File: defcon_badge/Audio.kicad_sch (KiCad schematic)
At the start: 16 parts, among them J20 PJ-320A, U20 TM8211, U21 TDA1308

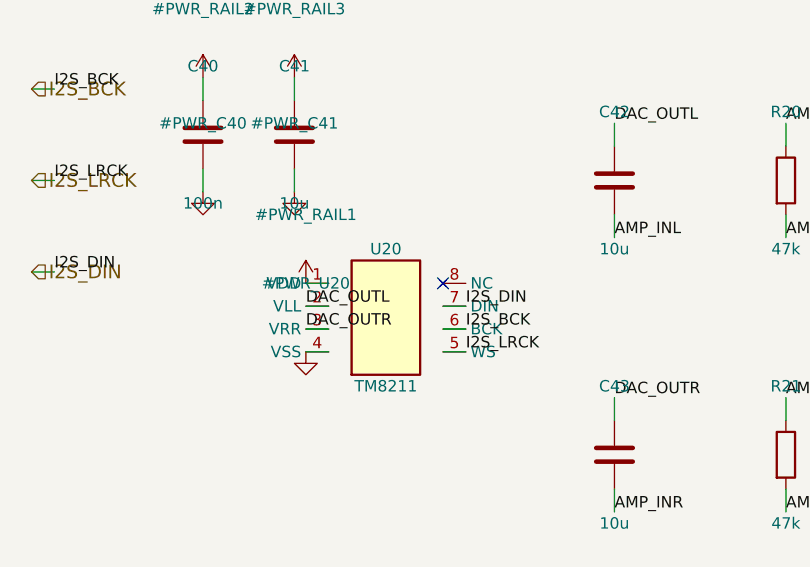
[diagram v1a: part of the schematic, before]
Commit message: Schematic: fix TM8211 DAC + SK9822 LED pinouts (datasheet-verified)
Both were ERC-invisible symbol bugs (wrong pin-number->signal mapping) that only
datasheet cross-reference catches — the kind that ships a non-functional board.

- TM8211 DAC (U20): the symbol pinout was scrambled. Verified against the Princeton
  PT8211 datasheet (+3 cross-checks): 1=BCK 2=WS 3=DIN 4=GND 5=VDD 6=LCH 7=NC 8=RCH.
  Fixed both symbol defs (gen_badge_lib + the inline copy in gen_audio_sheet) AND
  re-mapped the U20 wiring. Netlist verified: +3V3 was landing on the bit-clock pad;
  now every I2S/analog pin is on the correct pad.
- SK9822 LEDs (LED20-23): symbol pinout scrambled AND a 4-pad SK6812 footprint on a
  6-pin part. User chose 5050 (large/bright). Verified the SK9822 5050 datasheet
  pinout (Adafruit/Pololu/Normand): 1=DIN 2=CIN 3=GND 4=VDD 5=COUT 6=DOUT. Fixed the
  symbol + re-mapped the chain wiring; netlist verified (DOUT->next DIN, COUT->next
  CIN linked). Footprint set to badge:LED_SK9822_5050 — the 6-pad 5050 land pattern
  must be created in the PCB phase (no stock KiCad addressable-5050 footprint).
- Verified W25Q16 flash is a false alarm (already correct USON-8 + pinout).

ERC still 0 errors. The +4 warnings are the deliberate SK9822-footprint TODO.

Co-Authored-By: Claude Opus 4.8 (1M context) <noreply@anthropic.com>
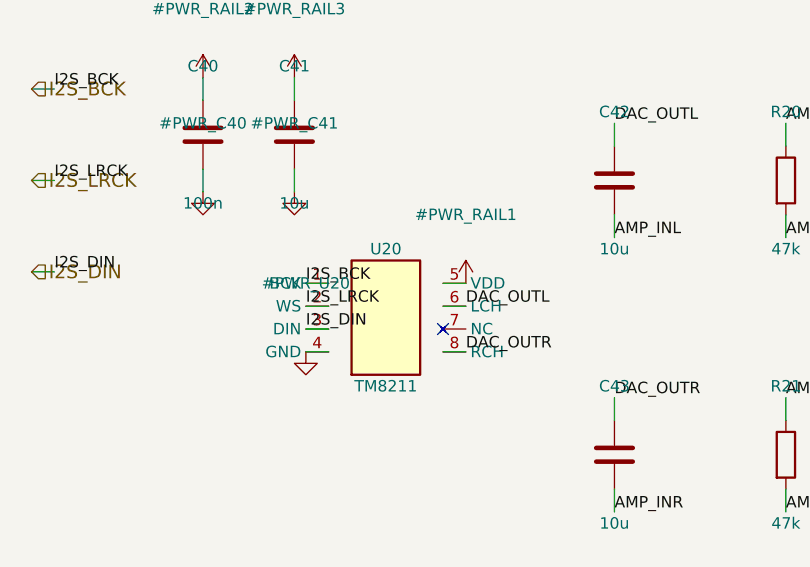
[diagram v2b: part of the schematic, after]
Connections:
- net +3V3: now also U20.5 (VDD); no longer U20.1 (VDD)
- net DAC_OUTL: now also U20.6 (LCH); no longer U20.2 (VLL)
- net DAC_OUTR: now also U20.8 (RCH); no longer U20.3 (VRR)
- net I2S_BCK: now also U20.1 (BCK); no longer U20.6 (BCK)
- net I2S_DIN: now also U20.3 (DIN); no longer U20.7 (DIN)
- net I2S_LRCK: now also U20.2 (WS); no longer U20.5 (WS)
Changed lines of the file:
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@@
 		(pin "3")
 		(pin "4")
+		(pin "5")
+		(pin "6")
+		(pin "7")
 		(pin "8")
-		(pin "7")
-		(pin "6")
-		(pin "5")
 		(instances
 			(project "defcon_badge"
@@
 	(symbol
 		(lib_id "power:+3V3")
-		(at 66.04 76.20 0)
-		(unit 1)
-		(body_style 1)
-		(exclude_from_sim no)
-		(in_bom yes)
-		(on_board yes)
-		(in_pos_files yes)
-		(dnp no)
-		(fields_autoplaced yes)
-		(property "Reference" "#PWR_RAIL1" (at 66.04 68.58 0) (effects (font (size 1.27 1.27))))
-		(property "Value" "+3V3" (at 66.04 83.82 0) (effects (font (size 1.27 1.27)) (hide yes)))
-		(property "Footprint" "" (at 66.04 76.20 0) (show_name no) (hide yes) (effects (font (size 1.27 1.27))))
-		(property "Datasheet" "" (at 66.04 76.20 0) (show_name no) (hide yes) (effects (font (size 1.27 1.27))))
-		(property "Description" "" (at 66.04 76.20 0) (show_name no) (hide yes) (effects (font (size 1.27 1.27))))
+		(at 83.82 76.20 0)
+		(unit 1)
+		(body_style 1)
+		(exclude_from_sim no)
+		(in_bom yes)
+		(on_board yes)
+		(in_pos_files yes)
+		(dnp no)
+		(fields_autoplaced yes)
+		(property "Reference" "#PWR_RAIL1" (at 83.82 68.58 0) (effects (font (size 1.27 1.27))))
+		(property "Value" "+3V3" (at 83.82 83.82 0) (effects (font (size 1.27 1.27)) (hide yes)))
+		(property "Footprint" "" (at 83.82 76.20 0) (show_name no) (hide yes) (effects (font (size 1.27 1.27))))
+		(property "Datasheet" "" (at 83.82 76.20 0) (show_name no) (hide yes) (effects (font (size 1.27 1.27))))
+		(property "Description" "" (at 83.82 76.20 0) (show_name no) (hide yes) (effects (font (size 1.27 1.27))))
 		(pin "1")
 		(instances
@@
 		)
 	)
-	(wire (pts (xy 68.58 76.20) (xy 66.04 76.20)) (stroke (width 0) (type default)))
+	(wire (pts (xy 81.28 76.20) (xy 83.82 76.20)) (stroke (width 0) (type default)))
 	(wire (pts (xy 68.58 83.82) (xy 66.04 83.82)) (stroke (width 0) (type default)))
 	(wire (pts (xy 54.61 55.88) (xy 54.61 53.34)) (stroke (width 0) (type default)))
@@
 	(wire (pts (xy 64.77 55.88) (xy 64.77 53.34)) (stroke (width 0) (type default)))
 	(wire (pts (xy 64.77 63.50) (xy 64.77 66.04)) (stroke (width 0) (type default)))
-	(wire (pts (xy 81.28 81.28) (xy 83.82 81.28)) (stroke (width 0) (type default)))
-	(wire (pts (xy 81.28 83.82) (xy 83.82 83.82)) (stroke (width 0) (type default)))
-	(wire (pts (xy 81.28 78.74) (xy 83.82 78.74)) (stroke (width 0) (type default)))
+	(wire (pts (xy 68.58 76.20) (xy 66.04 76.20)) (stroke (width 0) (type default)))
 	(wire (pts (xy 68.58 78.74) (xy 66.04 78.74)) (stroke (width 0) (type default)))
 	(wire (pts (xy 68.58 81.28) (xy 66.04 81.28)) (stroke (width 0) (type default)))
+	(wire (pts (xy 81.28 78.74) (xy 83.82 78.74)) (stroke (width 0) (type default)))
+	(wire (pts (xy 81.28 83.82) (xy 83.82 83.82)) (stroke (width 0) (type default)))
 	(wire (pts (xy 100.33 60.96) (xy 100.33 58.42)) (stroke (width 0) (type default)))
 	(wire (pts (xy 100.33 68.58) (xy 100.33 71.12)) (stroke (width 0) (type default)))
@@
 	(wire (pts (xy 35.56 64.77) (xy 38.10 64.77)) (stroke (width 0) (type default)))
 	(wire (pts (xy 35.56 74.93) (xy 38.10 74.93)) (stroke (width 0) (type default)))
-	(no_connect (at 81.28 76.20))
+	(no_connect (at 81.28 81.28))
 	(no_connect (at 208.28 77.47))
 	(no_connect (at 208.28 82.55))
-	(label "I2S_BCK" (at 83.82 81.28 0) (effects (font (size 1.27 1.27)) (justify left bottom)))
-	(label "I2S_LRCK" (at 83.82 83.82 0) (effects (font (size 1.27 1.27)) (justify left bottom)))
-	(label "I2S_DIN" (at 83.82 78.74 0) (effects (font (size 1.27 1.27)) (justify left bottom)))
-	(label "DAC_OUTL" (at 66.04 78.74 0) (effects (font (size 1.27 1.27)) (justify left bottom)))
-	(label "DAC_OUTR" (at 66.04 81.28 0) (effects (font (size 1.27 1.27)) (justify left bottom)))
+	(label "I2S_BCK" (at 66.04 76.20 0) (effects (font (size 1.27 1.27)) (justify left bottom)))
+	(label "I2S_LRCK" (at 66.04 78.74 0) (effects (font (size 1.27 1.27)) (justify left bottom)))
+	(label "I2S_DIN" (at 66.04 81.28 0) (effects (font (size 1.27 1.27)) (justify left bottom)))
+	(label "DAC_OUTL" (at 83.82 78.74 0) (effects (font (size 1.27 1.27)) (justify left bottom)))
+	(label "DAC_OUTR" (at 83.82 83.82 0) (effects (font (size 1.27 1.27)) (justify left bottom)))
 	(label "DAC_OUTL" (at 100.33 58.42 0) (effects (font (size 1.27 1.27)) (justify left bottom)))
 	(label "AMP_INL" (at 100.33 71.12 0) (effects (font (size 1.27 1.27)) (justify left bottom)))

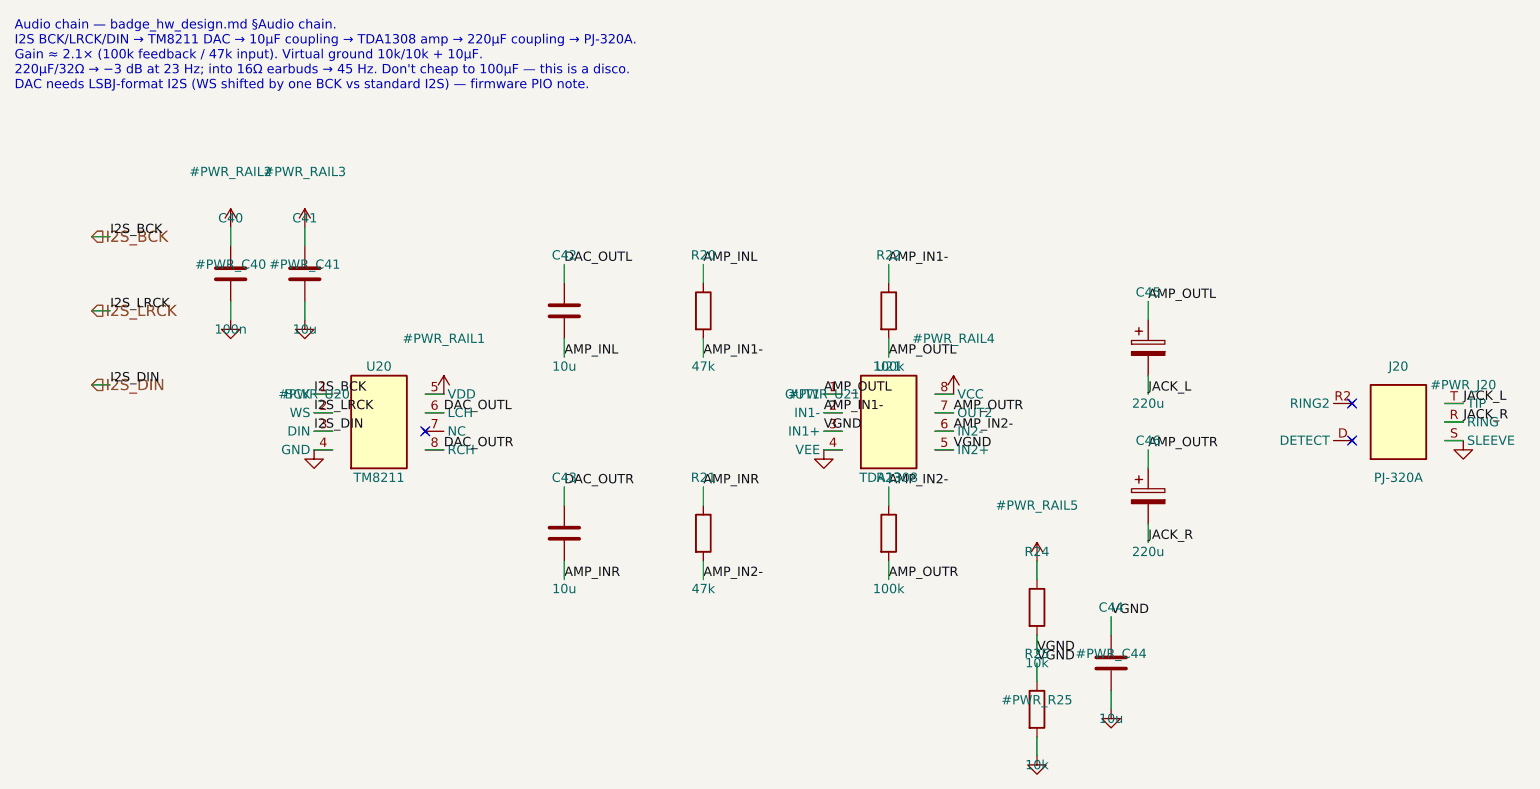
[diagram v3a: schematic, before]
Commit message: PCB: stereo audio jack + decoupling/thermal/clearance/placement fixes
J20 audio jack: the schematic specified a Thonkiconn WQP-PJ398SM footprint,
which is MONO (S/T/TN only) — wrong for a stereo badge (JACK_R had nowhere
to land). Swapped to CUI SJ1-3523N, a mainstream through-hole stereo TRS
jack with a verified KiCad footprint (TH survives plug/unplug better than
SMD). T=JACK_L, R=JACK_R, S=GND. Placed barrel overhanging the top edge,
repositioned to clear mounting hole H2, and stripped the footprint's
embedded Edge.Cuts (board has a straight edge here, no notch wanted).

C40 DAC decoupling: the TM8211 pinout fix moved U20's +3V3 from pad 1 to
pad 5; C40 was stranded 7.3mm away. Moved it adjacent to the new +3V3 pad.

U10 (TP4056) EP thermal vias: 0.2mm drilled holes tripped the 0.35mm
min-hole rule (and push into the expensive JLC drill tier). Enlarged to
0.30mm/0.60mm and relaxed board min-through-hole to 0.30mm (JLC standard).

D20 (IR LED): pad copper sat 0.075mm from the decorative sawtooth edge
(min 0.3mm). Nudged 0.4mm inboard → 0.48mm clearance. LED_0805 is
top-emitting, so edge proximity wasn't functionally needed.

R6 (RUN pull-up): was stranded 26mm from U3's RUN pin. Moved to a free
spot 3.1mm away; ratsnest 1395 -> 1360mm.

Verified: overlaps 0, courtyard 0, decoupling_max 3.47mm (<=3.5 gate),
DRC errors 0 except 28 inherent USB-C (J10) solder-mask bridges on the
qualified GCT footprint, schematic parity 0, ERC 0. 3D top/bottom renders
confirm jack orientation and single-side assembly.

Co-Authored-By: Claude Opus 4.8 (1M context) <noreply@anthropic.com>
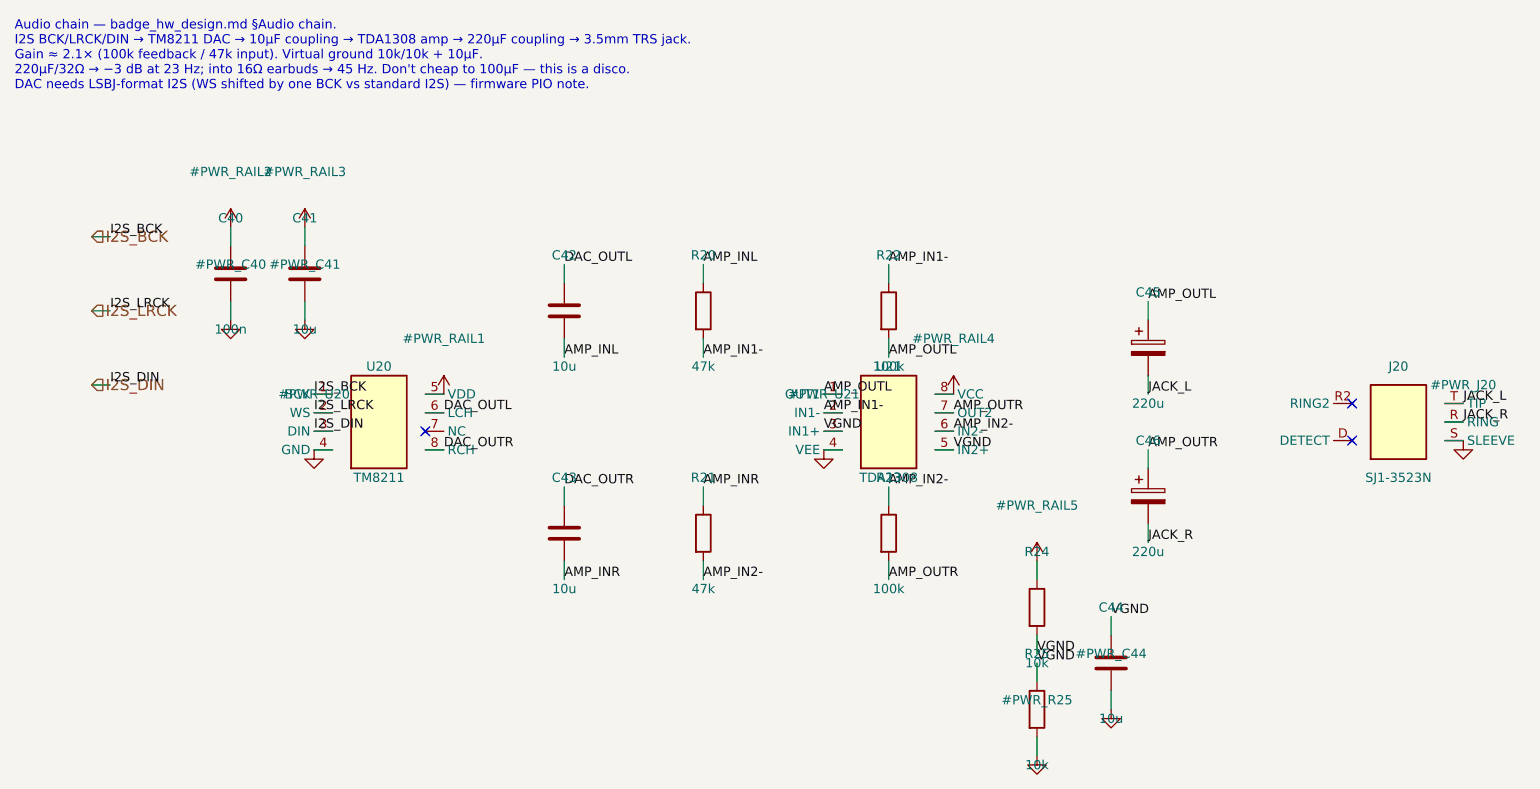
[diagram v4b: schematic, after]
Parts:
- J20: value PJ-320A -> SJ1-3523N; footprint Connector_Audio:Jack_3.5mm_QingPu_WQP-PJ398SM_Vertical_CircularHoles -> Connector_Audio:Jack_3.5mm_CUI_SJ1-3523N_Horizontal; LCSC C720466 -> (none); MPN PJ-320A -> SJ1-3523N
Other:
- note added: "Audio chain — badge_hw_design.md §Audio chain. I2S BCK/LRCK/DIN → TM8211 DAC → 10µF coupling → TDA1308 amp → 220µF coupling → 3.5mm TRS jack. Gain ≈ 2.1× (100k feedback / 47k input). Virtual ground 10k/10k + 10µF. 220µF/32Ω → −3 dB at 23 Hz; into 16Ω earbuds → 45 Hz. Don't cheap to 100µF — this is a disco. DAC needs LSBJ-format I2S (WS shifted by one BCK vs standard I2S) — firmware PIO note."
- note removed: "Audio chain — badge_hw_design.md §Audio chain. I2S BCK/LRCK/DIN → TM8211 DAC → 10µF coupling → TDA1308 amp → 220µF coupling → PJ-320A. Gain ≈ 2.1× (100k feedback / 47k input). Virtual ground 10k/10k + 10µF. 220µF/32Ω → −3 dB at 23 Hz; into 16Ω earbuds → 45 Hz. Don't cheap to 100µF — this is a disco. DAC needs LSBJ-format I2S (WS shifted by one BCK vs standard I2S) — firmware PIO note."
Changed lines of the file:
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@@
 		(comment 1 "TM8211 (PT8211 clone, 2.0-5.5V) — LSBJ-format 16-bit I2S in, stereo current-out")
 		(comment 2 "TDA1308 dual opamp headphone amp, ~2.1× gain (100k/47k), virtual ground 10k/10k")
-		(comment 3 "PJ-320A wired as TRS stereo, sleeve to GND, mic ring and detect left NC")
-	)
-	(text "Audio chain — badge_hw_design.md §Audio chain.\nI2S BCK/LRCK/DIN → TM8211 DAC → 10µF coupling → TDA1308 amp → 220µF coupling → PJ-320A.\nGain ≈ 2.1× (100k feedback / 47k input). Virtual ground 10k/10k + 10µF.\n220µF/32Ω → −3 dB at 23 Hz; into 16Ω earbuds → 45 Hz. Don't cheap to 100µF — this is a disco.\nDAC needs LSBJ-format I2S (WS shifted by one BCK vs standard I2S) — firmware PIO note." (exclude_from_sim no) (at 25.00 25.00 0) (effects (font (size 1.27 1.27)) (justify left top)))
+		(comment 3 "CUI SJ1-3523N 3.5mm stereo TRS jack, sleeve to GND (mic-ring/detect pins N/A on this part)")
+	)
+	(text "Audio chain — badge_hw_design.md §Audio chain.\nI2S BCK/LRCK/DIN → TM8211 DAC → 10µF coupling → TDA1308 amp → 220µF coupling → 3.5mm TRS jack.\nGain ≈ 2.1× (100k feedback / 47k input). Virtual ground 10k/10k + 10µF.\n220µF/32Ω → −3 dB at 23 Hz; into 16Ω earbuds → 45 Hz. Don't cheap to 100µF — this is a disco.\nDAC needs LSBJ-format I2S (WS shifted by one BCK vs standard I2S) — firmware PIO note." (exclude_from_sim no) (at 25.00 25.00 0) (effects (font (size 1.27 1.27)) (justify left top)))
 	(symbol
 		(lib_id "badge:TM8211")
@@
 		(fields_autoplaced yes)
 		(property "Reference" "J20" (at 214.63 72.39 0) (effects (font (size 1.27 1.27))))
-		(property "Value" "PJ-320A" (at 214.63 87.63 0) (effects (font (size 1.27 1.27))))
-		(property "Footprint" "Connector_Audio:Jack_3.5mm_QingPu_WQP-PJ398SM_Vertical_CircularHoles" (at 214.63 80.01 0) (show_name no) (hide yes) (effects (font (size 1.27 1.27))))
+		(property "Value" "SJ1-3523N" (at 214.63 87.63 0) (effects (font (size 1.27 1.27))))
+		(property "Footprint" "Connector_Audio:Jack_3.5mm_CUI_SJ1-3523N_Horizontal" (at 214.63 80.01 0) (show_name no) (hide yes) (effects (font (size 1.27 1.27))))
 		(property "Datasheet" "" (at 214.63 80.01 0) (show_name no) (hide yes) (effects (font (size 1.27 1.27))))
-		(property "Description" "3.5mm TRRS jack wired as TRS stereo" (at 214.63 80.01 0) (show_name no) (hide yes) (effects (font (size 1.27 1.27))))
-		(property "MPN" "PJ-320A" (at 214.63 80.01 0) (show_name no) (hide yes) (effects (font (size 1.27 1.27))))
-		(property "LCSC" "C720466" (at 214.63 80.01 0) (show_name no) (hide yes) (effects (font (size 1.27 1.27))))
+		(property "Description" "3.5mm stereo TRS jack (CUI SJ1-3523N), through-hole edge-mount" (at 214.63 80.01 0) (show_name no) (hide yes) (effects (font (size 1.27 1.27))))
+		(property "MPN" "SJ1-3523N" (at 214.63 80.01 0) (show_name no) (hide yes) (effects (font (size 1.27 1.27))))
+		(property "LCSC" "" (at 214.63 80.01 0) (show_name no) (hide yes) (effects (font (size 1.27 1.27))))
 		(pin "R2")
 		(pin "D")
